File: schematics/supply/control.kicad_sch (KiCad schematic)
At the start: 51 parts, among them J10 Conn_01x04_Pin, J11 Conn_01x04_Pin, J12 Conn_01x04_Pin, J13 USBASP, J14 Conn_01x05_Pin, J15 Conn_01x05_Pin, J9 Conn_01x04_Pin, M1 Fan, Q10 IRLML5203, Q6 IRLML0030, Q8 IRLML0030, SW1 EC11W****, SW2 SW_DPDT_x2, U17 ATmega328-A, U18 LM2904, U7 Display_1.18inch_st7535, Y4 HC-49SM, 16MHz

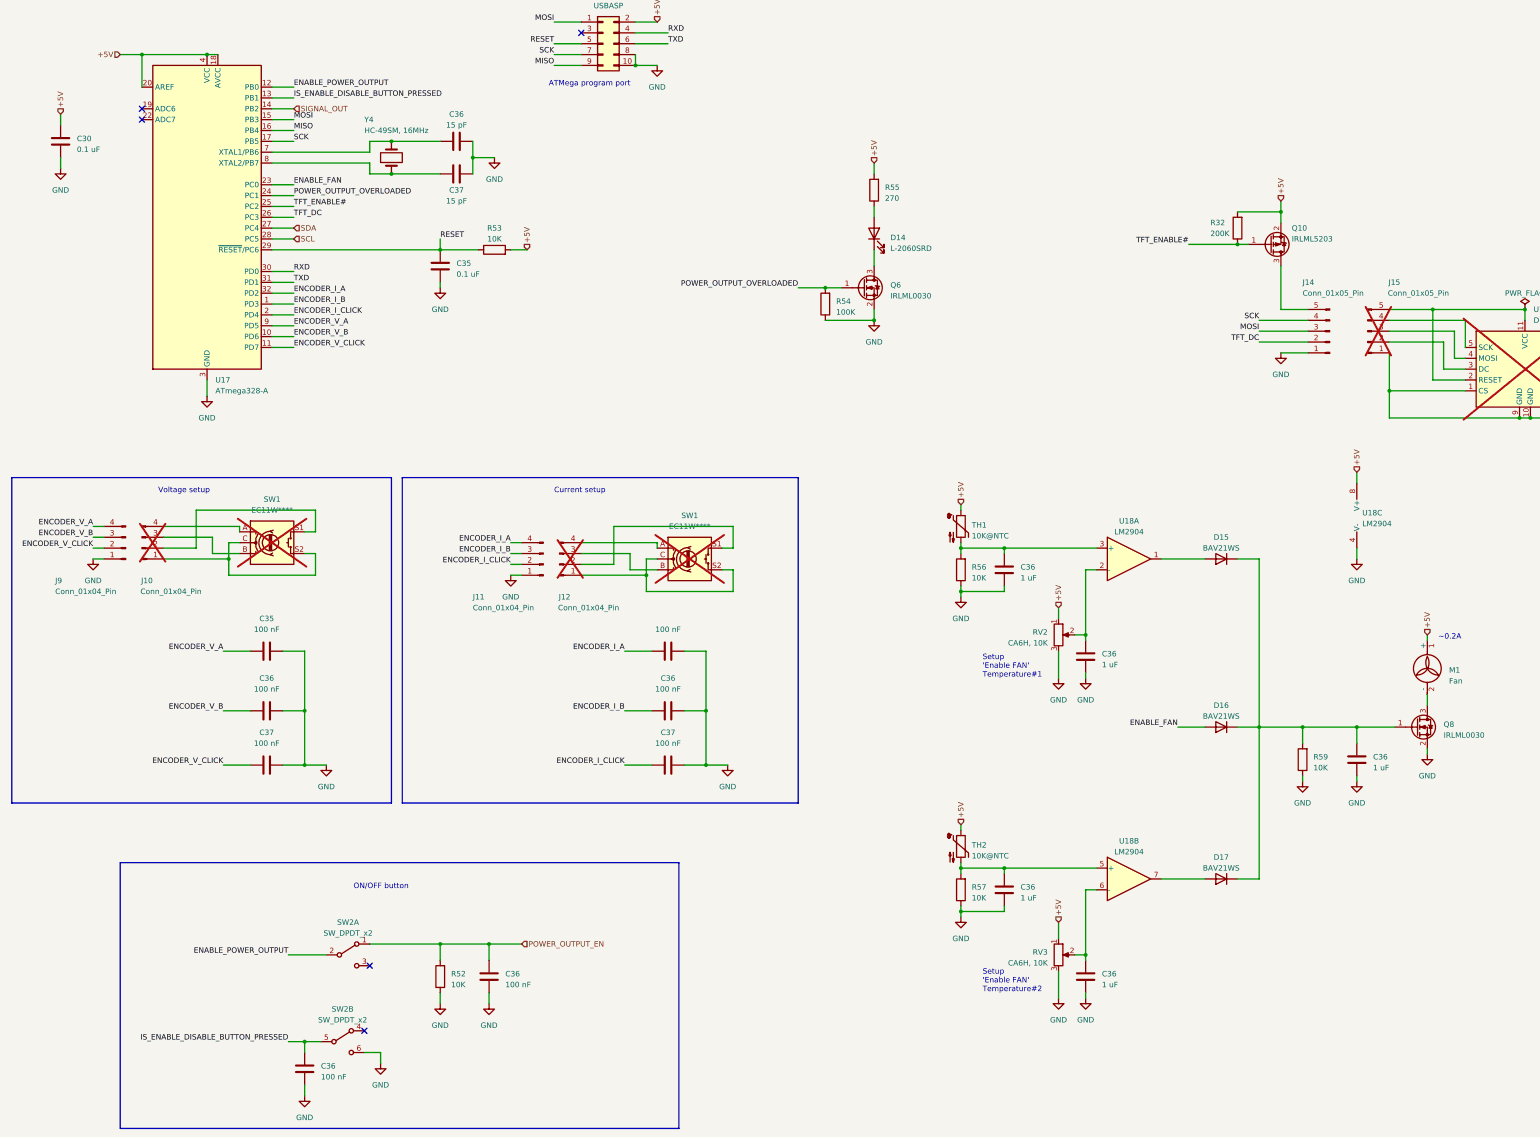
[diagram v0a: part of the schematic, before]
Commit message: prepare to replace ina228 to attiny16+ina169(?). ina228 is an intresting chip, but its too expensive and Im not sure I can buy it on ali
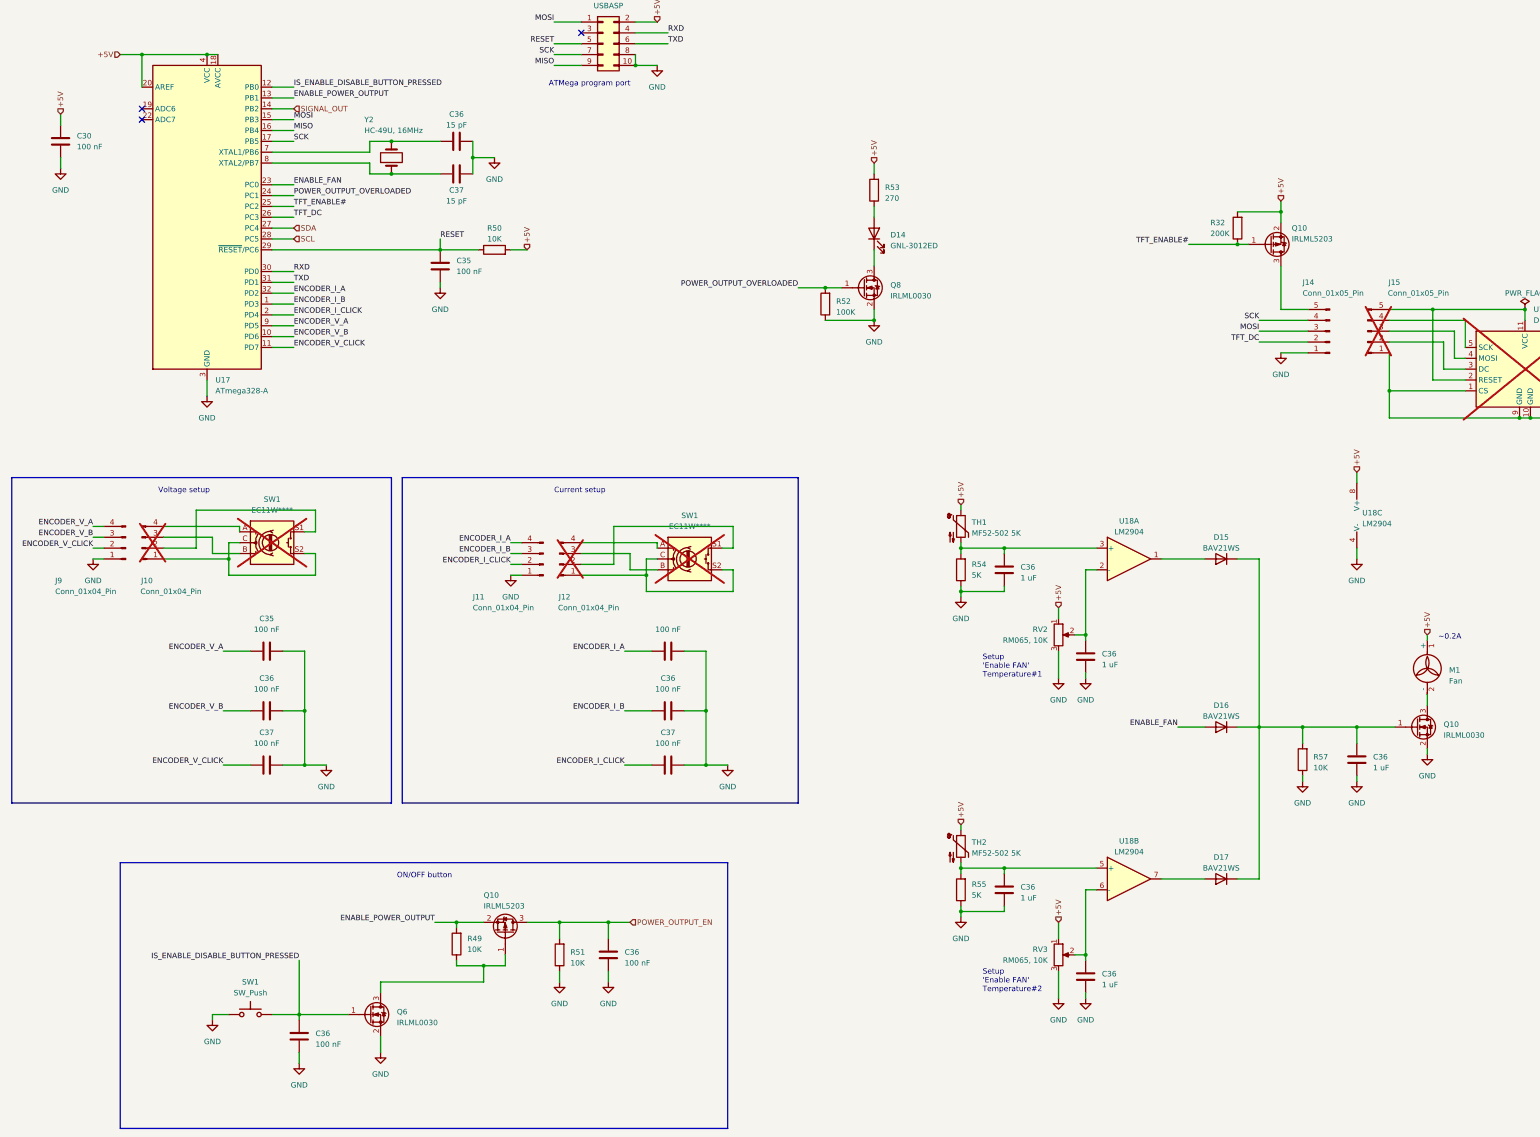
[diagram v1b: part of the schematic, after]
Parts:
- removed C36 (x2): 100 nF, Capacitor_SMD:C_0603_1608Metric, symbol Device:C
- removed R52: 10K, Resistor_SMD:R_0805_2012Metric, symbol Device:R
- removed SW2: SW_DPDT_x2, Connector_JST:JST_XH_B6B-XH-A_1x06_P2.50mm_Vertical, symbol Switch:SW_DPDT_x2
- added C36 (x2): 100 nF, Capacitor_SMD:C_0603_1608Metric, symbol Device:C
- added Q10: IRLML5203, Package_TO_SOT_SMD:SOT-23, symbol Transistor_FET:IRLML5203
- added Q6: IRLML0030, Package_TO_SOT_SMD:SOT-23, symbol Transistor_FET:IRLML0030
- added R49, R51: 10K, Resistor_SMD:R_0805_2012Metric, symbol Device:R
- added SW1: SW_Push, Connector_JST:JST_XH_B2B-XH-A_1x02_P2.50mm_Vertical, symbol Switch:SW_Push
- C30, C35: value 0.1 uF -> 100 nF
- D14: value L-2060SRD -> GNL-3012ED
- J15: now left out of the parts list
- R54: renamed from R56; value 10K -> 5K
- R55: renamed from R57; value 10K -> 5K
- RV2, RV3: value CA6H, 10K -> RM065, 10K; footprint Potentiometer_THT:Potentiometer_ACP_CA6-H2,5_Horizontal -> Potentiometer_THT:Potentiometer_Runtron_RM-065_Vertical
- TH1, TH2: value 10K@NTC -> MF52-502 5K
- U7: now in the parts list
- Y2: renamed from Y4; value HC-49SM, 16MHz -> HC-49U, 16MHz; footprint Crystal:Crystal_SMD_HC49-SD -> Crystal:Crystal_HC49-U_Vertical
- renumbered Q8 to Q10, Q6 to Q8, R53 to R50, R54 to R52, R55 to R53, R59 to R57
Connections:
- net ENABLE_POWER_OUTPUT: now also U17.13 (PB1), Q10.2 (S), R49.2; no longer U17.12 (PB0)
- net GND: now also C36.1, C36.1, Q6.2 (S), R51.1, SW1.1
- net IS_ENABLE_DISABLE_BUTTON_PRESSED: now also U17.12 (PB0), C36.2, Q6.1 (G), SW1.2; no longer U17.13 (PB1)
- net POWER_OUTPUT_EN: now also C36.2, Q10.3 (D), R51.2
- new net: Q10.1 (G), Q6.3 (D), R49.1
- no-connect marks 5 -> 3

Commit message: Prepare to move USB ports to a few millimenters outside
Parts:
- removed C36 (x2): 100 nF, Capacitor_SMD:C_0603_1608Metric, symbol Device:C
- removed Q6: IRLML0030, Package_TO_SOT_SMD:SOT-23, symbol Transistor_FET:IRLML0030
- removed R49, R51: 10K, Resistor_SMD:R_0805_2012Metric, symbol Device:R
- added C31, C38, C39: 100 nF, Capacitor_SMD:C_0603_1608Metric, symbol Device:C
- added D15, D16, D17: BAV21WS, Diode_SMD:D_SOD-323F, symbol Device:D
- added J14: USBASP, Connector_PinHeader_2.54mm:PinHeader_2x05_P2.54mm_Vertical, symbol Connector_Generic:Conn_02x05_Odd_Even
- added JP7: Jumper_2_Open, TestPoint:TestPoint_2Pads_Pitch2.54mm_Drill0.8mm, symbol Jumper:Jumper_2_Open
- added R50, R58, R59, R60, R61: 10K, Resistor_SMD:R_0805_2012Metric, symbol Device:R
- added R53, R55: 4K7, Resistor_SMD:R_0805_2012Metric, symbol Device:R
- added U18: ATtiny1616-M, Package_DFN_QFN:VQFN-20-1EP_3x3mm_P0.4mm_EP1.7x1.7mm, symbol MCU_Microchip_ATtiny:ATtiny1616-M
- added X1: CSX-750FCC, 16MHz, Oscillator:Oscillator_SMD_Abracon_ASE-4Pin_3.2x2.5mm, symbol Oscillator:SG-211
- renumbered D15 to D18, D16 to D19, D17 to D20, J14 to J15, J15 to J16, Q8 to Q6, Q10 to Q9, R50 to R49, R52 to R51, R53 to R52, R54 to R56, R55 to R57, R57 to R62, SW1 to SW3, U18 to U20
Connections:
- net +5V: now also Q10.2 (S), SW3.1, C31.1, C39.1, J14.2 (Pin_2), R50.2, R53.2, R55.2, U18.4 (VCC), U18.6 (PA5), X1.1 (~{ST}), X1.4 (Vcc)
- net ENABLE_POWER_OUTPUT: now also Q10.1 (G), R58.1; no longer Q10.2 (S)
- net GND: now also C31.2, C38.2, C39.2, J14.10 (Pin_10), J14.8 (Pin_8), R58.2, R59.1, R60.1, R61.1, U18.21 (GND), U18.3 (GND), X1.2 (GND); no longer SW3.1
- net SCL: now also R53.1, U18.14 (PB0)
- net SDA: now also R55.1, U18.13 (PB1)
- net IS_ENABLE_DISABLE_BUTTON_PRESSED renamed IS_ONOFF_BUTTON_PRESSED
- net IS_ONOFF_BUTTON_PRESSED: now also D17.2 (A), R59.2
- net POWER_OUTPUT_EN: no longer names the net of Q10.3 (D)
- net POWER_OUTPUT_EN: now also D15.2 (A)
- net POWER_OUTPUT_OVERLOADED renamed POWER_OUTPUT_OVERLOADED_LED
- net POWER_OUTPUT_OVERLOADED_LED: now also U18.17 (PC2); no longer U17.24 (PC1)
- net RESET renamed RESET#
- new net: JP7.2 (B), X1.3 (OUT)
- new net ATTINY_MISO: J14.9 (Pin_9), U18.1 (PA2)
- new net ATTINY_MOSI: J14.1 (Pin_1), U18.20 (PA1)
- new net ATTINY_RXD: J14.4 (Pin_4), U18.11 (PB3)
- new net ATTINY_SCK: J14.7 (Pin_7), JP7.1 (A), U18.2 (PA3)
- new net ATTINY_TXD: J14.6 (Pin_6), U18.12 (PB2)
- new net POWER_OUTPUT_CURRENT_SENSE: U18.8 (PA7)
- new net POWER_OUTPUT_FB: D15.1 (K), D16.1 (K), D17.1 (K), R61.2
- new net POWER_OUTPUT_IC_FB: D16.2 (A), R60.2, U18.16 (PC1)
- new net POWER_OUTPUT_RESET#: C38.1, J14.5 (Pin_5), R50.1, U17.24 (PC1), U18.19 (~{RESET}/PA0)
- new net POWER_OUTPUT_VOLT_SENSE: U18.10 (PB4)
- no-connect marks 3 -> 9
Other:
- note added: "ATTiny program port"
- note added: "vdd cap"
- note added: "vref cap"
- moved on the sheet: C36, D18, D19, D20, J15, J16, M1, Q10, Q9, R32, R56, R57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

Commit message: little changes in schematics
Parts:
- renumbered R49 to R45, R50 to R46, R51 to R47, R52 to R48, R53 to R49, R55 to R51, R56 to R52, R57 to R53, R58 to R54, R59 to R55, R60 to R56, R61 to R57, R62 to R58, U17 to U16, U18 to U17, U20 to U19

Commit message: prepare to add current measurement for a middle-current 5V and 3.3V lines
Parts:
- U19: value LM2904 -> LM158DR
- renumbered Y2 to X2
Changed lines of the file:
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@@
       (effects (font (size 1.27 1.27)))
     )
-    (property "Value" "LM2904" (at 425.45 285.75 0)
+    (property "Value" "LM158DR" (at 425.45 285.75 0)
       (effects (font (size 1.27 1.27)))
     )
@@
       (effects (font (size 1.27 1.27)))
     )
-    (property "Value" "LM2904" (at 425.45 360.68 0)
+    (property "Value" "LM158DR" (at 425.45 360.68 0)
       (effects (font (size 1.27 1.27)))
     )
@@
   (symbol (lib_id "Device:Crystal") (at 106.68 54.61 90) (unit 1)
     (in_bom yes) (on_board yes) (dnp no)
-    (property "Reference" "Y2" (at 100.33 45.72 90)
+    (property "Reference" "X2" (at 100.33 45.72 90)
       (effects (font (size 1.27 1.27)) (justify right))
     )
@@
       (project "supply"
         (path "/1e139717-fcd1-4008-a6ea-4c993845e928/ce2ff71a-422a-4b17-921a-2433d38ec044"
-          (reference "Y2") (unit 1)
+          (reference "X2") (unit 1)
         )
       )
@@
   (symbol (lib_id "Amplifier_Operational:LM2904") (at 481.33 281.94 0) (unit 3)
     (in_bom yes) (on_board yes) (dnp no) (fields_autoplaced)
-    (property "Reference" "U19" (at 480.06 281.305 0)
-      (effects (font (size 1.27 1.27)) (justify left))
-    )
-    (property "Value" "LM2904" (at 480.06 283.845 0)
-      (effects (font (size 1.27 1.27)) (justify left))
-    )
+    (property "Reference" "U19" (at 480.06 280.67 0)
+      (effects (font (size 1.27 1.27)) (justify left))
+    )
+    (property "Value" "LM158DR" (at 480.06 283.21 0)
+      (effects (font (size 1.27 1.27)) (justify left))
+    )

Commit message: Added over-voltage protection to 5V line
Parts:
- renumbered D14 to D16, D15 to D17, D16 to D18, D17 to D19, D18 to D20, D19 to D21, D20 to D22, RV2 to RV3, RV3 to RV4, U16 to U17, U17 to U18, U19 to U20, X2 to X1, X1 to X2
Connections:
- net +5V renamed +5V_VSYS

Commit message: Fixed problem with 20V on one leg of comparator
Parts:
- renumbered C30 to C32, C31 to C33, C35 to C37, C36 to C38, C37 to C39, C38 to C40, C39 to C41, D16 to D19, D17 to D20, D18 to D21, D19 to D22, D20 to D23, D21 to D24, D22 to D25, JP7 to JP6, RV3 to RV4, RV4 to RV5

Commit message: Some changes in board - Im preparing it to production
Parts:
- removed J15: Conn_01x05_Pin, Connector_JST:JST_XH_B5B-XH-A_1x05_P2.50mm_Vertical, symbol Connector:Conn_01x05_Pin
- removed J16: Conn_01x05_Pin, symbol Connector:Conn_01x05_Pin
- removed U7: Display_1.18inch_st7535, Library:Display_1.18inch_st7735, symbol My_Library:Display_1.18inch_st7535
- added J15: Conn_01x06_Pin, Connector_JST:JST_XH_B6B-XH-A_1x06_P2.50mm_Vertical, symbol Connector:Conn_01x06_Pin
- added J16: Conn_01x06_Pin, symbol Connector:Conn_01x06_Pin
- added U19: Display_2.2inch_ili9341, symbol My_Library:Display_2.2inch_ili9341
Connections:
- net GND: now also J15.6 (Pin_6)
- net MISO: now also J15.5 (Pin_5)
- net MOSI: now also J15.3 (Pin_3)
- net SCK: now also J15.4 (Pin_4)
- net TFT_DC: now also J15.2 (Pin_2)
- net at Q10.3 (D): now also J15.1 (Pin_1)
- new net: J16.1 (Pin_1), U19.1 (VCC), U19.4 (RESET#), U19.8 (LED)
- new net: J16.2 (Pin_2), U19.5 (DC)
- new net: J16.3 (Pin_3), U19.6 (MOSI)
- new net: J16.4 (Pin_4), U19.7 (SCK)
- new net: J16.5 (Pin_5), U19.9 (MISO)
- new net: J16.6 (Pin_6), U19.2 (GND), U19.3 (CS)
